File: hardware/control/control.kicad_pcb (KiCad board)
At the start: 2 copper layers, 110 x 70 mm, 58 parts, among them J1 Conn_01x05_Male, J2 CANPWR, J3 CANGND, J4 RJ45, J5 RJ45, J6 Conn_02x03_Odd_Even, Q1 BSS123, SW1 next, SW2 select, U1 2.048V, U2 AP63200WU, U3 PIC18F27Q84, U4 TLE9250VSJXUMA1, Y1 10Mhz

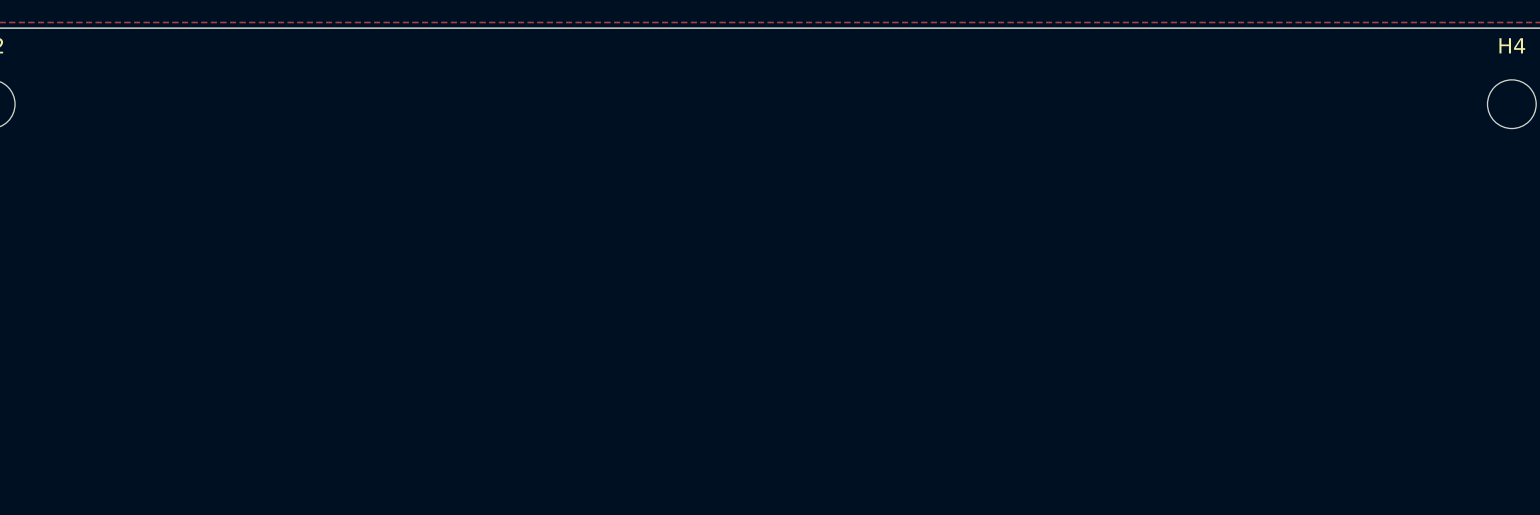
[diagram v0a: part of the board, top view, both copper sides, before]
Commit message: Place holes and connectors on control board to match DC/DC
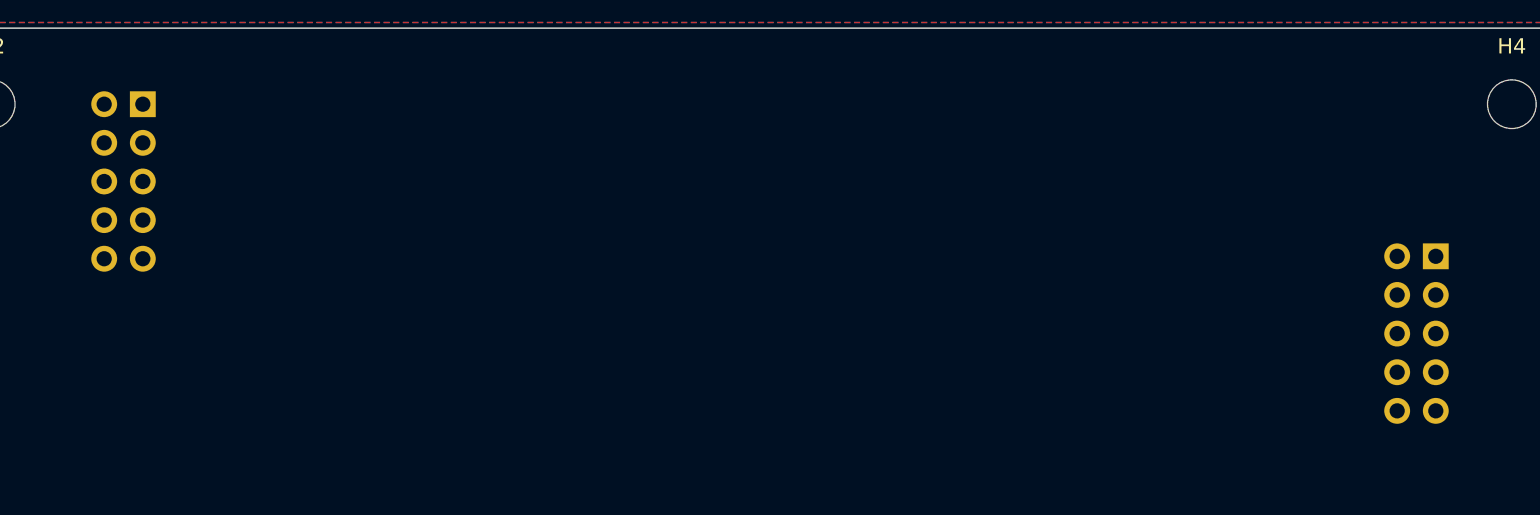
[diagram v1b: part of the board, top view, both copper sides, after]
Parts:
- added J7: DCDC-PWM, Connector_PinHeader_2.54mm:PinHeader_2x05_P2.54mm_Vertical, B.Cu at (65.0, 85.0)
- added J8: DCDC-MEASURES, Connector_PinHeader_2.54mm:PinHeader_2x05_P2.54mm_Vertical, B.Cu at (150.0, 95.0)
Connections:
- U3 pad 2: /PWM_V -> PWM_V
- U3 pad 21: /AL2 -> AL2
- U3 pad 22: /AL1 -> AL1
- U3 pad 25: /BATT1_ON -> BATT1_ON
- U3 pad 26: /BATT2_ON -> BATT2_ON
- U3 pad 4: Net-(R1-Pad2) -> TH

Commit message: Route control board. Will need a separate board for display.
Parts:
- removed R1: 10K, Resistor_SMD:R_0805_2012Metric_Pad1.20x1.40mm_HandSolder
- removed TH1: NTC10K, Resistor_SMD:R_0201_0603Metric_Pad0.64x0.40mm_HandSolder
- C13, C14, C5, C6, D3, Q1, R13, R14, R18, U4, Y1: moved to B.Cu
- J1: footprint Connector_PinHeader_2.54mm:PinHeader_1x05_P2.54mm_Vertical -> Connector_PinHeader_2.54mm:PinHeader_1x05_P2.54mm_Horizontal; moved to B.Cu
- J4, J5: footprint Connector_RJ:RJ45_Amphenol_54602-x08_Horizontal -> local:RJ45_Amphenol_54602-x08_Horizontal_handsolder
- R10, R11, R12, R9: footprint Resistor_SMD:R_0805_2012Metric_Pad1.20x1.40mm_HandSolder -> Resistor_THT:R_Axial_DIN0309_L9.0mm_D3.2mm_P12.70mm_Horizontal; moved to B.Cu
- moved F2 332.8 mm to (57.9, 104.1), turned to 180 degrees
- moved J3 321.1 mm to (81.3, 116.3), turned to 180 degrees
- moved R13 318.9 mm to (87.1, 95.5)
- moved R14 295.4 mm to (86.0, 103.7), turned to 180 degrees
- moved J2 291.4 mm to (85.1, 116.3), turned to 180 degrees
- moved Q1 290.3 mm to (86.1, 99.7), turned to 90 degrees
- moved R4 285.3 mm to (110.7, 94.0), turned to 90 degrees
- moved C14 283.0 mm to (85.1, 121.9), turned to 90 degrees
- moved J4 282.1 mm to (92.5, 121.4)
- moved R8 278.4 mm to (132.3, 87.6), turned to 180 degrees
- moved D3 278.4 mm to (82.3, 126.5), turned to 180 degrees
- moved R18 276.3 mm to (105.0, 110.7), turned to -90 degrees
- moved C1 275.0 mm to (106.7, 98.3), turned to 90 degrees
- moved J6 274.4 mm to (113.9, 109.5), turned to -90 degrees
- moved R5 273.1 mm to (128.4, 84.3)
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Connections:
- U3 pad 21: AL2 -> AL1
- U3 pad 22: AL1 -> AL2
- U3 pad 6: GND -> ~{RST_DISP}
- U3 pad 7: ~{RST_DISP} -> GND
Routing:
- net +5V: track 37.8 -> 291.7 mm, vias 0 -> 3
- net BATT2_ON: track 0.00 -> 173.7 mm, vias 0 -> 2
- net BATT1_ON: track 0.00 -> 163.6 mm, vias 0 -> 2
- net /PWM: track 0.00 -> 144.7 mm, vias 0 -> 1
- net /PWM_OFF: track 0.00 -> 86.1 mm, vias 0 -> 2
- net /PWM_OK: track 0.00 -> 79.5 mm, vias 0 -> 2
- net TH: track 0.00 -> 69.0 mm
- net /CANGND: track 0.00 -> 68.1 mm, vias 0 -> 2
- net PWM_V: track 0.00 -> 66.6 mm
- net /CANL: track 0.00 -> 65.4 mm
- net /CANH: track 0.00 -> 63.9 mm
- net /!CANOK: track 0.00 -> 58.1 mm, vias 0 -> 2
- net Net-(D2-Pad2): track 0.00 -> 56.0 mm
- net Net-(C14-Pad1): track 0.00 -> 55.6 mm
- net /CANTX: track 0.00 -> 52.0 mm, vias 0 -> 1
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- added copper zone on B.Cu, net /CANGND
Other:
- outline, holes or cut-outs redrawn

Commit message: Re-route PCBs to move RJ45 connectors on bottom, saving a bit of stack size.
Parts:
- C10, C12, C2, C3, C4, C8, C9, J2, J3, J4, J5, J6, L1, R15, R16, R17, R2, R3, R6, R7, U2: moved to B.Cu
- C13, C14, D3, Q1, R12, R13, R14, R18, U4: moved to F.Cu
- R11: footprint Resistor_THT:R_Axial_DIN0309_L9.0mm_D3.2mm_P12.70mm_Horizontal -> Resistor_SMD:R_0805_2012Metric_Pad1.20x1.40mm_HandSolder; moved to F.Cu
- moved R17 361.3 mm to (61.2, 106.2), turned to 180 degrees
- moved SW1 355.4 mm to (60.0, 125.0)
- moved R15 339.1 mm to (61.2, 102.6)
- moved SW2 333.5 mm to (60.0, 110.0)
- moved R16 332.4 mm to (61.2, 135.9), turned to 180 degrees
- moved D3 75.2 mm to (150.4, 94.5), turned to 90 degrees
- moved C14 65.8 mm to (146.1, 97.0), turned to 180 degrees
- moved J3 63.5 mm to (140.5, 93.2), turned to 90 degrees
- moved J2 58.6 mm to (140.5, 97.0), turned to 90 degrees
- moved R9 57.8 mm to (84.1, 118.1)
- moved R10 57.8 mm to (88.4, 118.1)
- moved J4 55.7 mm to (145.5, 104.4), turned to -90 degrees
- moved R12 48.6 mm to (110.6, 94.5)
- moved C7 45.0 mm to (95.2, 108.2), turned to -90 degrees
- moved R14 44.8 mm to (129.3, 115.1), turned to 90 degrees
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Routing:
- net BATT2_ON: track 173.7 -> 54.3 mm, vias 2 -> 0
- net BATT1_ON: track 163.6 -> 49.6 mm, vias 2 -> 0
- net BTN_IN: track 7.56 -> 96.5 mm, vias 0 -> 1
- net /PWM: track 144.7 -> 58.6 mm, vias 1 -> 0
- net Net-(D2-Pad2): track 56.0 -> 3.20 mm
- net AL1: track 15.4 -> 56.1 mm
- net /~{PAC_DOWN}: track 15.6 -> 55.2 mm, vias 0 -> 2
- net AL2: track 27.0 -> 55.5 mm
- net /PGC: track 9.34 -> 36.3 mm
- net /PWM_OFF: track 86.1 -> 62.8 mm, vias 2 -> 0
- net /PGD: track 10.7 -> 33.8 mm
- net /CAN_PWR: track 8.18 -> 30.8 mm, vias 1 -> 0
- net SDA: track 36.9 -> 59.4 mm, vias 0 -> 1
- net /PWM_OK: track 79.5 -> 57.2 mm, vias 2 -> 0
- net GND: track 44.9 -> 28.1 mm, vias 8 -> 7
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- added copper zone on F.Cu, net /CANGND
- removed copper zone on B.Cu, net /CANGND

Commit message: Adjust PWM resistor divider to better match NCP5091B mid-state input voltage.
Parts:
- R10: value 10K -> 8.1K
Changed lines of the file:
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@@
       (effects (font (size 1 1) (thickness 0.15)) (justify mirror))
     )
-    (fp_text value "10K" (at 6.35 -2.72 90) (layer "B.Fab")
+    (fp_text value "8.1K" (at 6.35 -2.72 90) (layer "B.Fab")
       (effects (font (size 1 1) (thickness 0.15)) (justify mirror))
     )
